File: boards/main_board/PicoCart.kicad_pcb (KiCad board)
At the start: 2 copper layers, 99.8 x 99.5 mm, 29 parts, among them J1 MSX Bus (Odd-Even), J2 Micro_SD_Card, J3 UART, J4 DEBUG, J5 MSX Debug, J6 Pico Debug, J7 Ground Pins, J8 Ground Pins, J9 Edge Connector, U1 LD1117S33TR_SOT223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

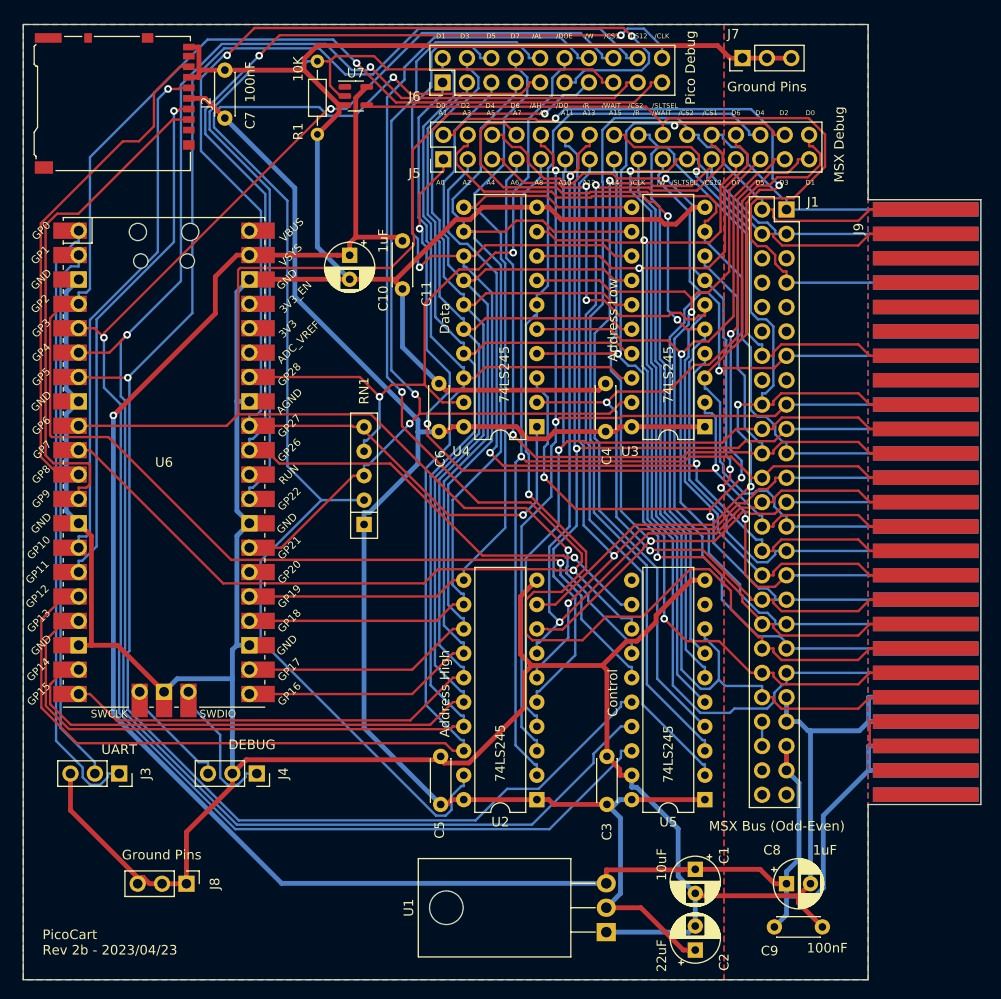
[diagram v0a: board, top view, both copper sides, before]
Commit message: Added 16 data lines
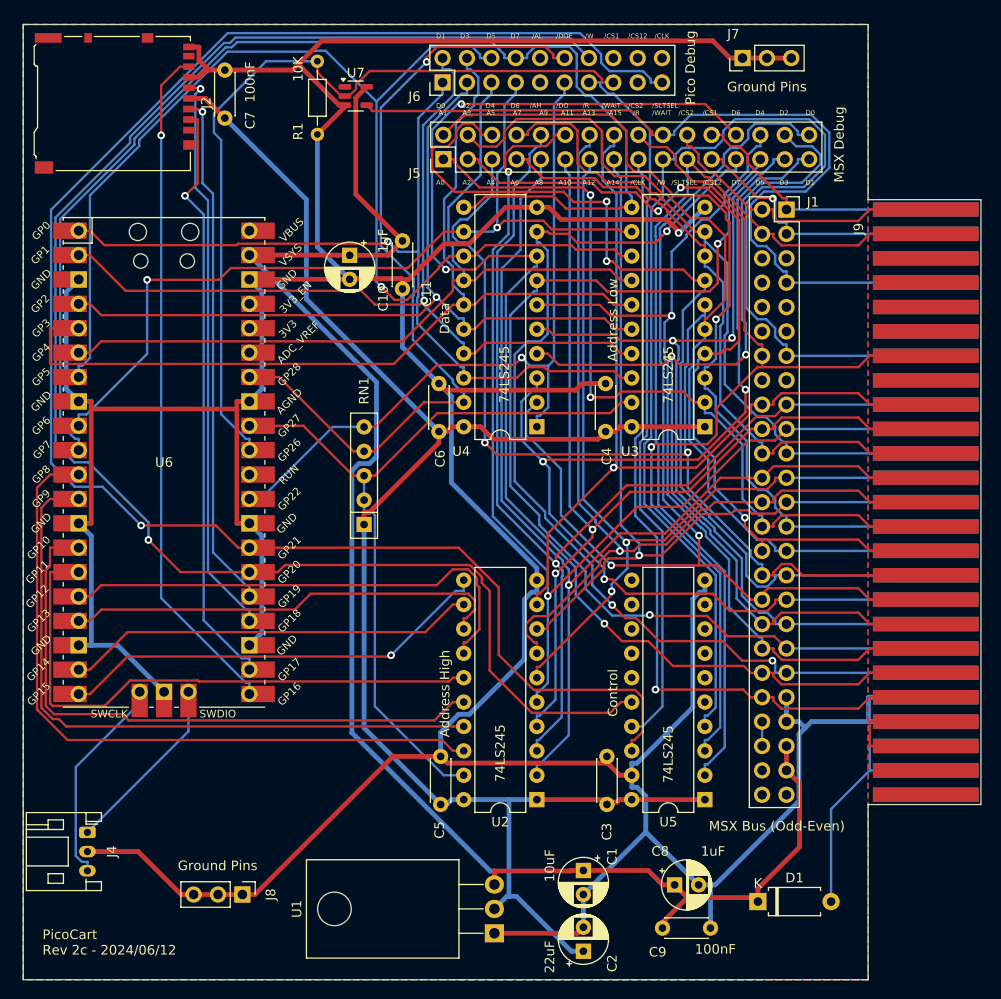
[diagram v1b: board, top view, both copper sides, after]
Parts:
- removed J3: UART, Connector_PinSocket_2.54mm:PinSocket_1x03_P2.54mm_Vertical
- added D1: D, Diode_THT:D_A-405_P7.62mm_Horizontal, F.Cu at (184.0, 132.4)
- J4: footprint Connector_PinSocket_2.54mm:PinSocket_1x03_P2.54mm_Vertical -> Connector_JST:JST_PH_S3B-PH-K_1x03_P2.00mm_Horizontal
- moved J4 18.7 mm to (114.2, 125.2)
- moved C9 11.7 mm to (174.1, 135.1)
- moved C1 11.7 mm to (165.8, 129.1)
- moved C2 11.7 mm to (165.8, 137.5)
- moved C8 11.7 mm to (175.3, 130.6)
- moved U1 11.7 mm to (156.6, 135.7)
- moved J8 5.93 mm to (130.3, 131.6)
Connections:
- J9 pad 45: +5V -> Net-(D1-A)
- J9 pad 47: +5V -> Net-(D1-A)
- RN1 pad 2: /AHOE -> /AOE
- RN1 pad 3: /ALOE -> /AOE
- U2 pad 11: /I_D7 -> /I_D15
- U2 pad 12: /I_D6 -> /I_D14
- U2 pad 13: /I_D5 -> /I_D13
- U2 pad 14: /I_D4 -> /I_D12
- U2 pad 15: /I_D3 -> /I_D11
- U2 pad 16: /I_D2 -> /I_D10
- U2 pad 17: /I_D1 -> /I_D9
- U2 pad 18: /I_D0 -> /I_D8
- U2 pad 19: /AHOE -> /AOE
- U3 pad 19: /ALOE -> /AOE
- U5 pad 12: I_CLK -> unconnected-(U5-B6-Pad12)
- U5 pad 13: /I_WRITE -> unconnected-(U5-B5-Pad13)
- U5 pad 14: /I_READ -> unconnected-(U5-B4-Pad14)
- U5 pad 15: /I_SLTSEL -> unconnected-(U5-B3-Pad15)
- U5 pad 16: /I_CS12 -> /I_WRITE
- U5 pad 17: /I_CS2 -> /I_READ
- U5 pad 18: /I_CS1 -> /I_SLTSEL
- U5 pad 2: /E_CS1 -> /E_SLTSEL
- U5 pad 3: /E_CS2 -> /E_READ
- U5 pad 4: /E_CS12 -> /E_WRITE
- U5 pad 5: /E_SLTSEL -> unconnected-(U5-A3-Pad5)
- U5 pad 6: /E_READ -> unconnected-(U5-A4-Pad6)
- U5 pad 7: /E_WRITE -> unconnected-(U5-A5-Pad7)
- U5 pad 8: E_CLK -> unconnected-(U5-A6-Pad8)
- U6 pad 1: UART_TX -> /I_D0
- U6 pad 10: /I_WRITE -> /I_D7
- U6 pad 11: SPI_MISO -> /I_D8
- U6 pad 12: SPI_CS -> /I_D9
- U6 pad 14: SPI_SCK -> /I_D10
- U6 pad 15: SPI_MOSI -> /I_D11
- U6 pad 16: /I_D0 -> /I_D12
- U6 pad 17: /I_D1 -> /I_D13
- U6 pad 19: /I_D2 -> /I_D14
- U6 pad 2: UART_RX -> /I_D1
- U6 pad 20: /I_D3 -> /I_D15
- U6 pad 21: /I_D4 -> SPI_MISO
- U6 pad 22: /I_D5 -> SPI_CS
- U6 pad 24: /I_D6 -> SPI_SCK
- U6 pad 25: /I_D7 -> SPI_MOSI
- U6 pad 26: /AHOE -> /I_WRITE
- U6 pad 27: /ALOE -> /I_SLTSEL
- U6 pad 29: /DOE -> /DOUT
- U6 pad 31: I_CLK -> /I_WAIT
- U6 pad 32: /DOUT -> /AOE
- U6 pad 34: /I_WAIT -> /DOE
- U6 pad 4: /I_SLTSEL -> /I_D2
- U6 pad 5: /I_CS1 -> /I_D3
- U6 pad 6: /I_CS2 -> /I_D4
- U6 pad 7: /I_CS12 -> /I_D5
- U6 pad 9: /I_READ -> /I_D6
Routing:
- net /I_CS2: track 189.4 -> 0.00 mm, vias 2 -> 0
- net /I_CS12: track 188.6 -> 0.00 mm, vias 1 -> 0
- net /I_CS1: track 172.9 -> 0.00 mm, vias 2 -> 0
- net I_CLK: track 138.5 -> 0.00 mm, vias 3 -> 0
- net /AHOE: track 137.4 -> 0.00 mm, vias 1 -> 0
- net /ALOE: track 100.4 -> 0.00 mm, vias 2 -> 0
- net /E_CS1: track 112.6 -> 26.9 mm, vias 1 -> 0
- net /AOE: track 0.00 -> 82.3 mm
- net /E_CS2: track 112.0 -> 30.7 mm
- net /I_D8: track 0.00 -> 74.2 mm
- net /E_CS12: track 101.4 -> 27.5 mm
- net /I_D9: track 0.00 -> 69.9 mm
- net /DOUT: track 143.1 -> 74.8 mm, vias 3 -> 1
- net /I_D0: track 154.6 -> 89.1 mm, vias 0 -> 1
- net /I_D10: track 0.00 -> 64.6 mm
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- added copper zone on F.Cu, net GND
- removed copper zone on F.Cu, net +3.3V
- removed copper zone on F.Cu, net +5V
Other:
- board text added: "PicoCart Rev 2c - 2024/06/12"
- board text removed: "PicoCart Rev 2b - 2023/04/23"
